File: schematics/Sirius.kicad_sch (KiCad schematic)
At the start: 10 parts, among them J1 DE9_Plug, U1 W65C02SxP, U2 W65C51NxPL, U3 6526, U4 MAX232, U5 74LS138, U6 27C64, U7 CY62256-70PC, U8 7404, X1 GTXO-14T

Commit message: Re-worked schematics. Still lot of work to be done.
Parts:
- removed U2: W65C51NxPL, Package_LCC:PLCC-28, symbol PCM_65xx-library:W65C51NxPL
- removed U3: 6526, Package_DIP:DIP-40_W15.24mm, symbol PCM_65xx-library:6526
- removed U4: MAX232, symbol Interface_UART:MAX232
- removed U6: 27C64, Package_DIP:DIP-28_W15.24mm, symbol Memory_EPROM:27C64
- removed U7: CY62256-70PC, Package_DIP:DIP-28_W15.24mm, symbol Memory_RAM:CY62256-70PC
- removed U8: 7404, symbol 74xx_IEEE:7404
- removed X1: GTXO-14T, Oscillator:Oscillator_DIP-14, symbol Oscillator:GTXO-14T
- added U2: W65C51NxP, Package_DIP:DIP-28_W15.24mm, symbol PCM_65xx-library:W65C51NxP
- added U3: 2764, Package_DIP:DIP-28_W15.24mm, symbol Memory_EPROM:2764
- added U4: 74LS138, symbol 74xx:74LS138
- added U6, U7, U8, U9: ~, symbol custom_parts:CY6264
- added X1: TFT680, Oscillator:Oscillator_DIP-14, symbol Oscillator:TFT680
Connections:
- net GND: now also U3.14 (GND), U4.4 (E1), U4.5 (E2), U4.8 (GND), X1.7 (GND); no longer U1.21 (VSS)
- net at U1.4 (~{IRQ}): now also U2.26 (~{IRQ})
- net at U1.34 (R/~{W}): now also U2.28 (R/~{W})
- net at U1.39 (ϕ2): now also U2.27 (ϕ2)
- net at U1.40 (~{RES}): now also U2.4 (~{RES})
- net at U5.15 (O0): now also U2.2 (CS1)
- net at U5.6 (E3): now also U4.9 (O6)
- net at U1.37 (ϕ0): now also X1.8 (OUT)
- net A0: no longer names the net of U1.9 (A0)
- net A1: no longer names the net of U1.10 (A1)
- net A10: no longer names the net of U1.19 (A10)
- net A11: no longer names the net of U1.20 (A11)
- net A12: no longer names the net of U1.22 (A12)
- net A13: no longer names the net of U1.23 (A13)
- net A14: no longer names the net of U1.24 (A14)
- net A15: no longer names the net of U1.25 (A15)
- net A2: no longer names the net of U1.11 (A2)
- net A3: no longer names the net of U1.12 (A3)
- net A4: no longer names the net of U1.13 (A4)
- net A5: no longer names the net of U1.14 (A5)
- net A6: no longer names the net of U1.15 (A6)
- net A7: no longer names the net of U1.16 (A7)
- net A8: no longer names the net of U1.17 (A8)
- net A9: no longer names the net of U1.18 (A9)
- net D0: no longer names the net of U1.33 (D0)
- net D1: no longer names the net of U1.32 (D1)
- net D2: no longer names the net of U1.31 (D2)
- net D3: no longer names the net of U1.30 (D3)
- net D4: no longer names the net of U1.29 (D4)
- net D5: no longer names the net of U1.28 (D5)
- net D6: no longer names the net of U1.27 (D6)
- net D7: no longer names the net of U1.26 (D7)
- net Vcc renamed VCC
- net VCC: now also U2.15 (VCC), U3.28 (VCC), U4.16 (VCC), U4.6 (E3), X1.1 (EN), X1.14 (Vcc); no longer U1.8 (VDD)
- new net: U3.20 (~{CE}), U4.7 (O7)
- new net VDD: U1.8 (VDD)
- new net VSS: U1.21 (VSS), U2.1 (VSS), U2.3 (~{CS2})
- no-connect marks 8 -> 0

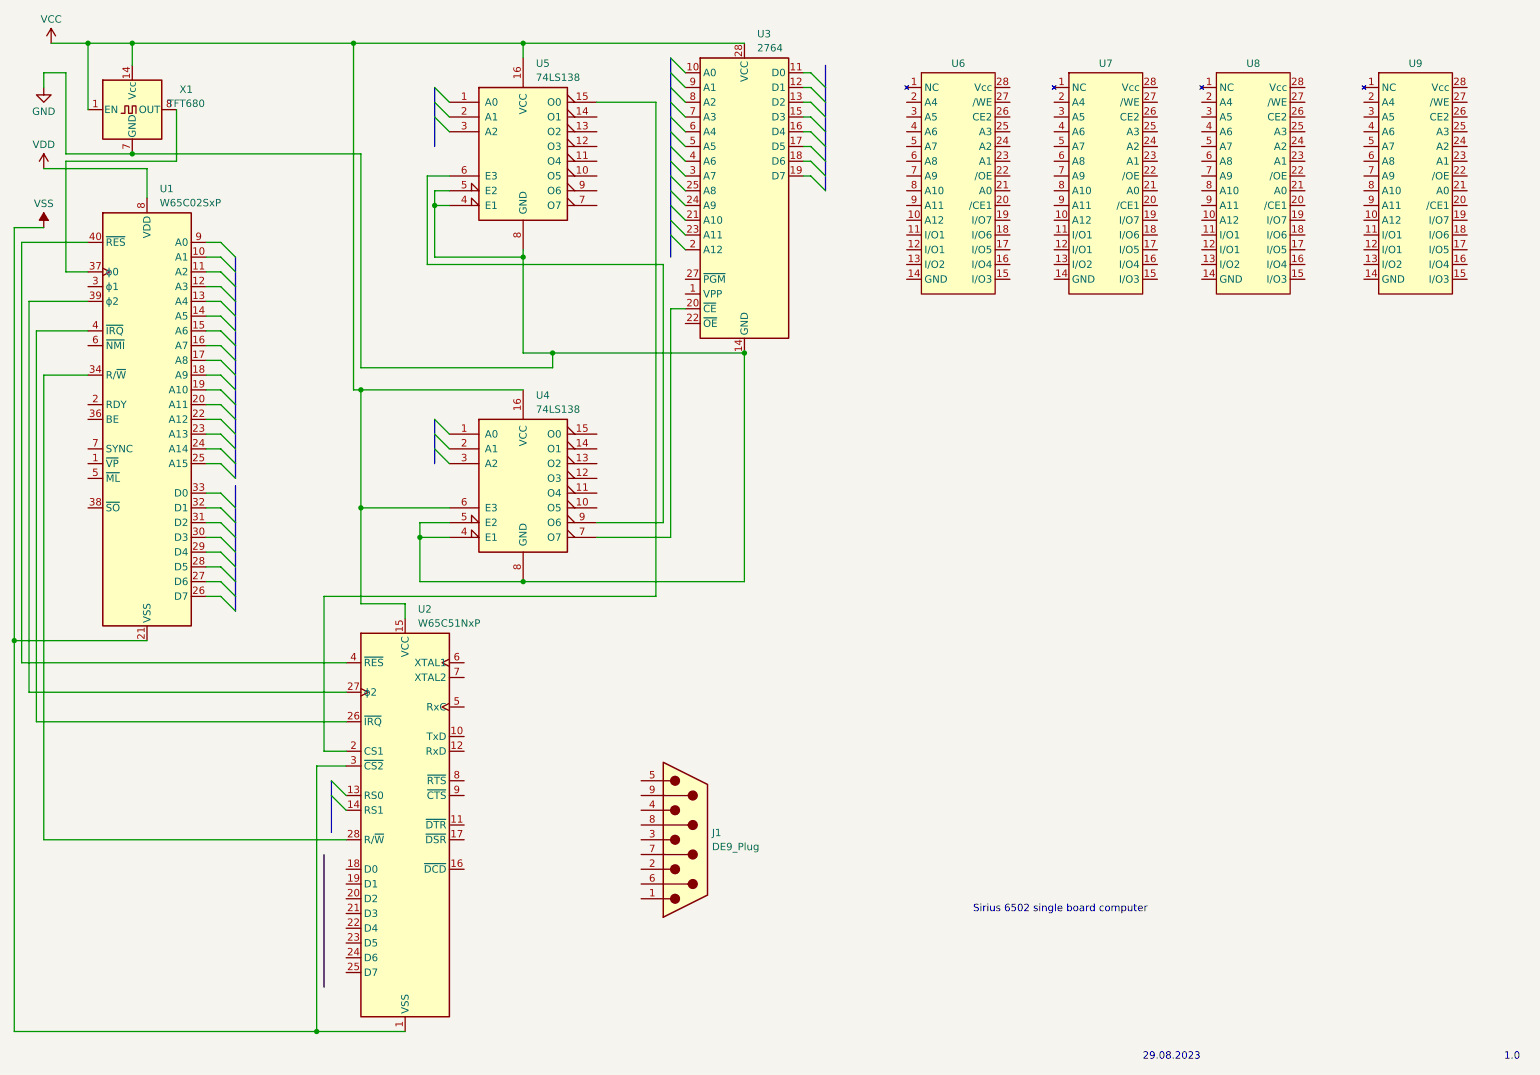
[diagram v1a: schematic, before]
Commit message: Added RAM along with connectivity. Still issues with using the Bus.
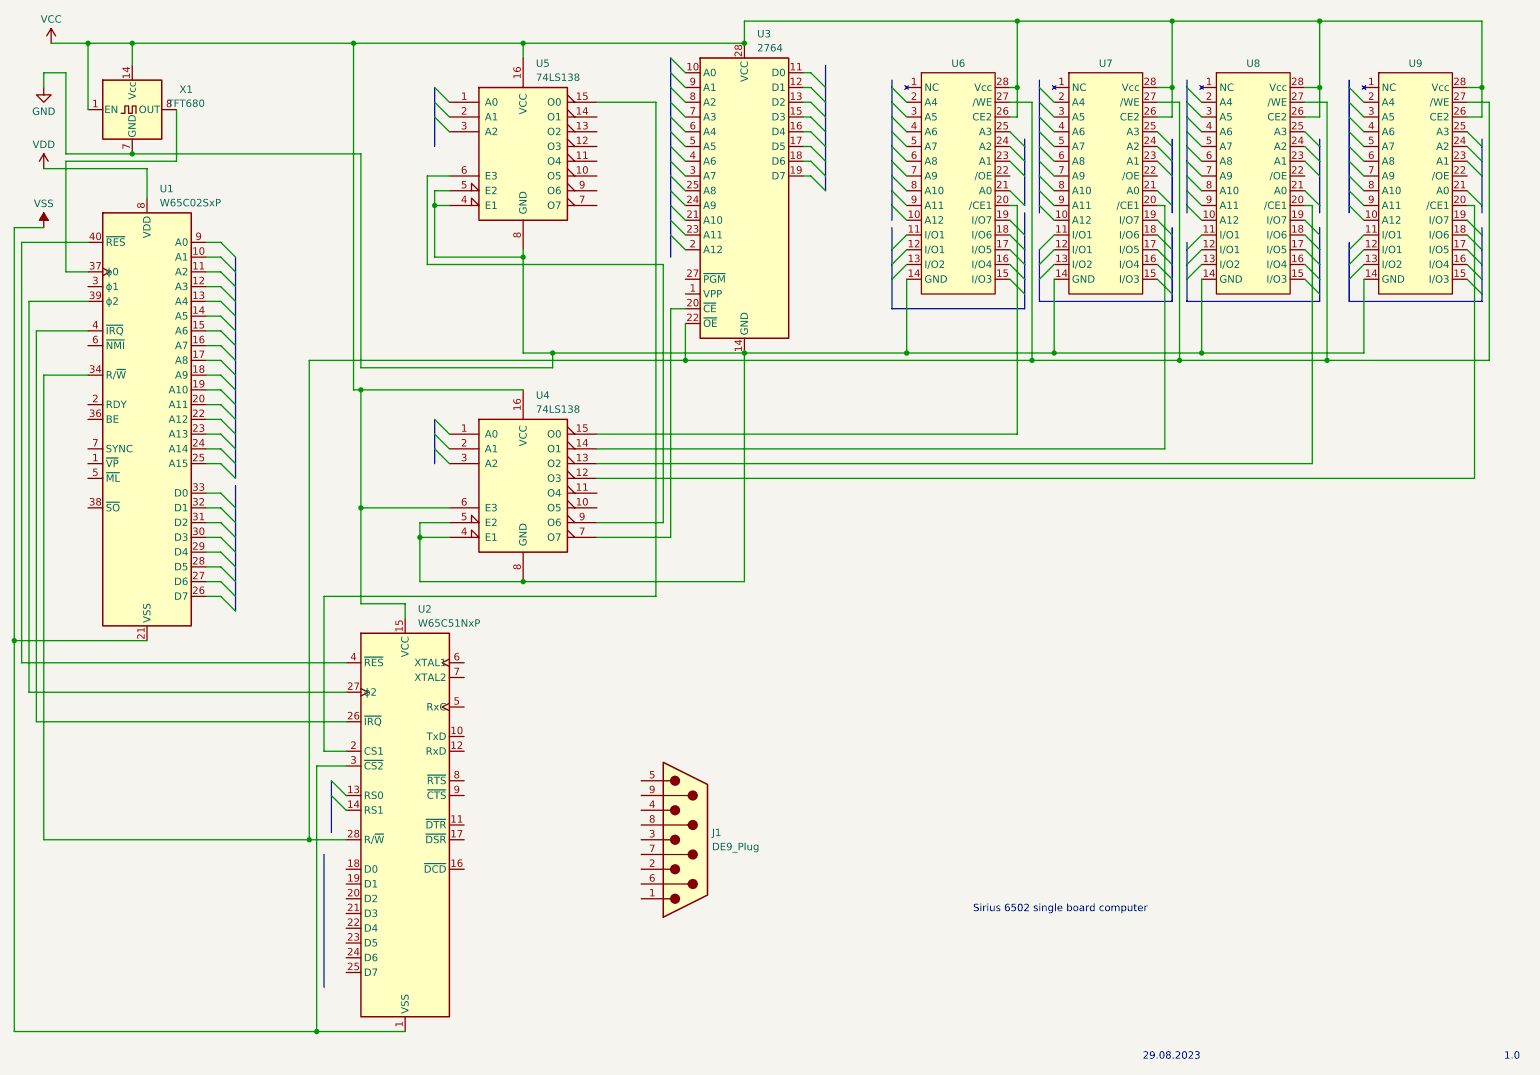
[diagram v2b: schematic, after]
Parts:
- U4, U5: footprint (none) -> Package_DIP:DIP-16_W7.62mm
- U6, U7, U8, U9: footprint (none) -> Package_DIP:DIP-28_W15.24mm
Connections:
- net GND: now also U6.14 (GND), U7.14 (GND), U8.14 (GND), U9.14 (GND)
- net VCC: now also U6.26 (CE2), U6.28 (Vcc), U7.26 (CE2), U7.28 (Vcc), U8.26 (CE2), U8.28 (Vcc), U9.26 (CE2), U9.28 (Vcc)
- net at U9.20 (/CE1): now also U4.12 (O3)
- net at U9.27 (/WE): now also U1.34 (R/~{W}), U2.28 (R/~{W}), U3.22 (~{OE}), U6.27 (/WE), U7.27 (/WE), U8.27 (/WE)
- net at U7.20 (/CE1): now also U4.14 (O1)
- net at U8.20 (/CE1): now also U4.13 (O2)
- net at U4.15 (O0): now also U6.20 (/CE1)

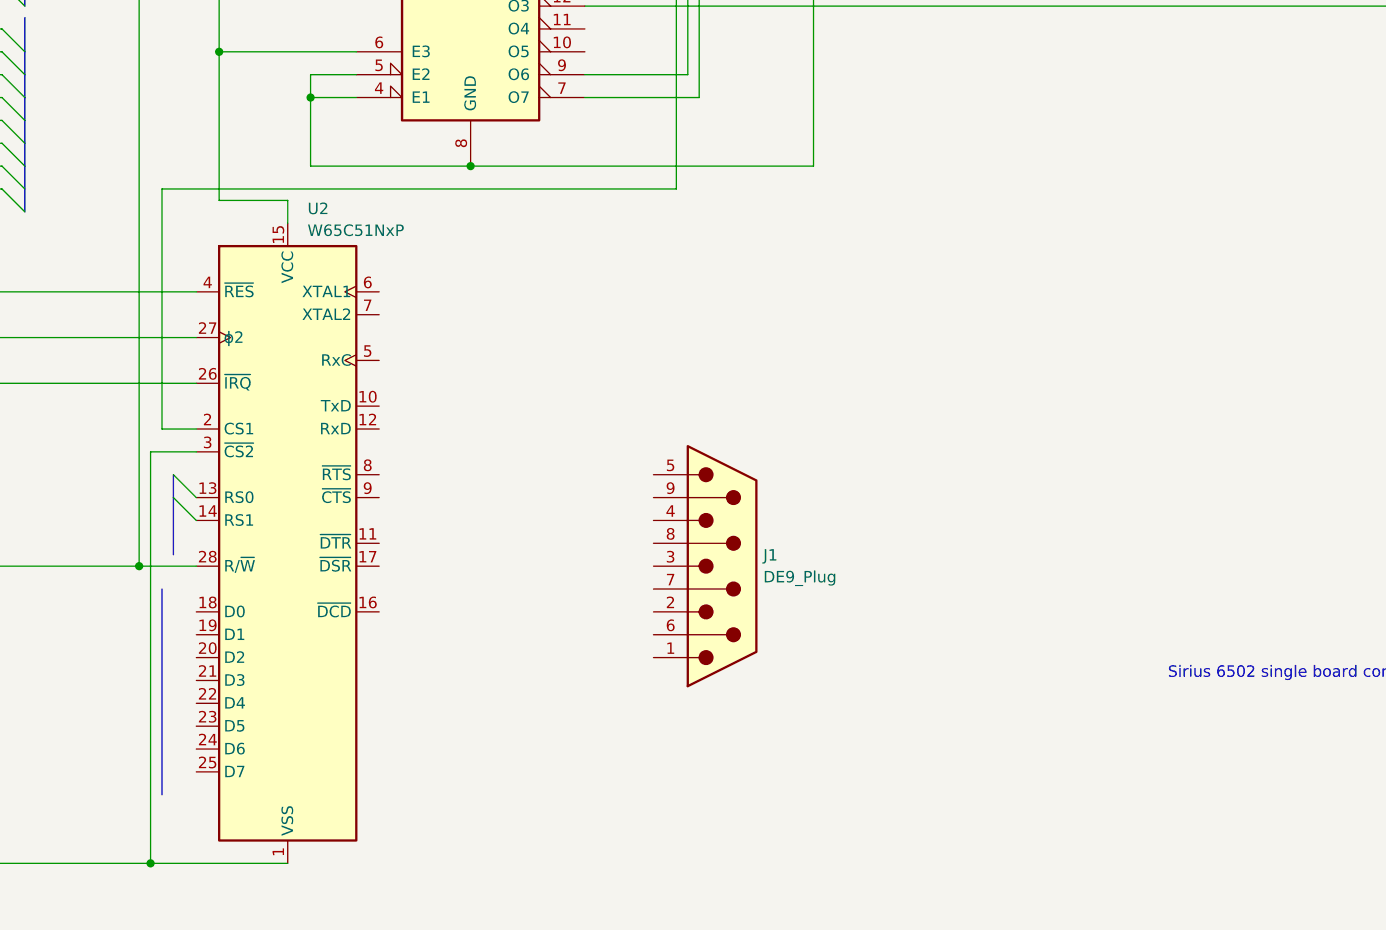
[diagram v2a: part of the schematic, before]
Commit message: Added rs232 parts. Still some caps to add.
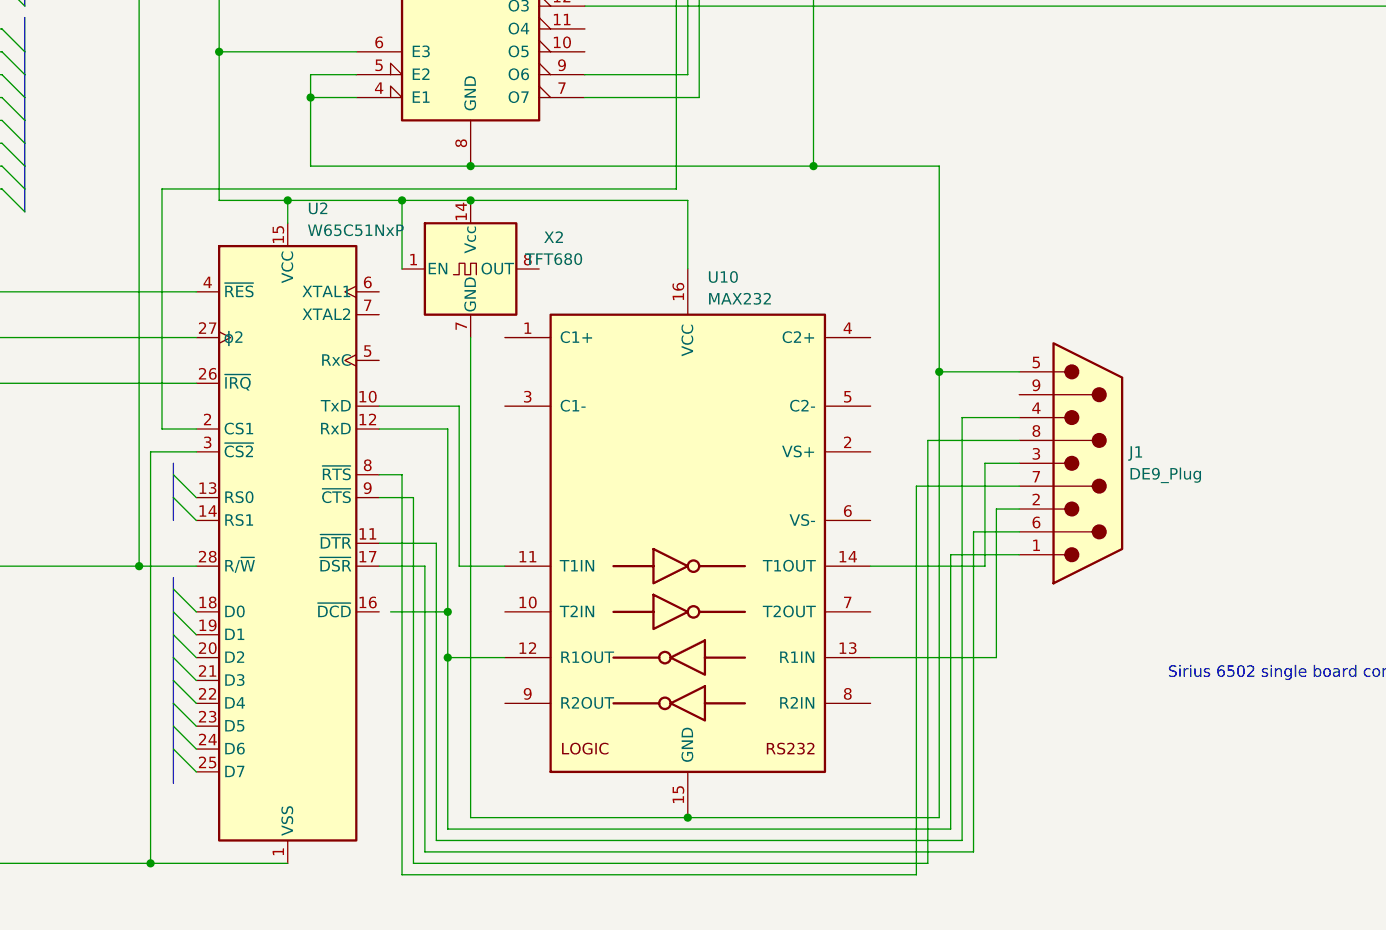
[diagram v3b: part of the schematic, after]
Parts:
- added U10: MAX232, Package_DIP:DIP-16_W7.62mm, symbol Interface_UART:MAX232
- added X2: TFT680, Oscillator:Oscillator_DIP-14, symbol Oscillator:TFT680
- J1: footprint (none) -> Connector_Dsub:DSUB-9_Male_EdgeMount_P2.77mm
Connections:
- net GND: now also J1.5, U10.15 (GND), X2.7 (GND)
- net VCC: now also U10.16 (VCC), X2.1 (EN), X2.14 (Vcc)
- net at U2.10 (TxD): now also U10.11 (T1IN)
- net at U2.11 (~{DTR}): now also J1.4
- net at U2.12 (RxD): now also J1.1, U10.12 (R1OUT)
- net at U2.17 (~{DSR}): now also J1.6
- net at U2.8 (~{RTS}): now also J1.7
- net at U2.9 (~{CTS}): now also J1.8
- net at J1.2: now also U10.13 (R1IN)
- net at J1.3: now also U10.14 (T1OUT)
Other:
- moved on the sheet: J1
